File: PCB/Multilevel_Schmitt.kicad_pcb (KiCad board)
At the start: 2 copper layers, 32 x 102 mm, 24 parts, among them J1 Conn_02x03_Counter_Clockwise, J2 Conn_01x03, J3 Conn_01x08_Female, J4 Conn_01x08_Female, J5 Conn_01x02, Q1 BS170, U1 ATtiny84-20PU, U2 74HC14, U3 MCP1700-2502E_TO92, U4 74HC4051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

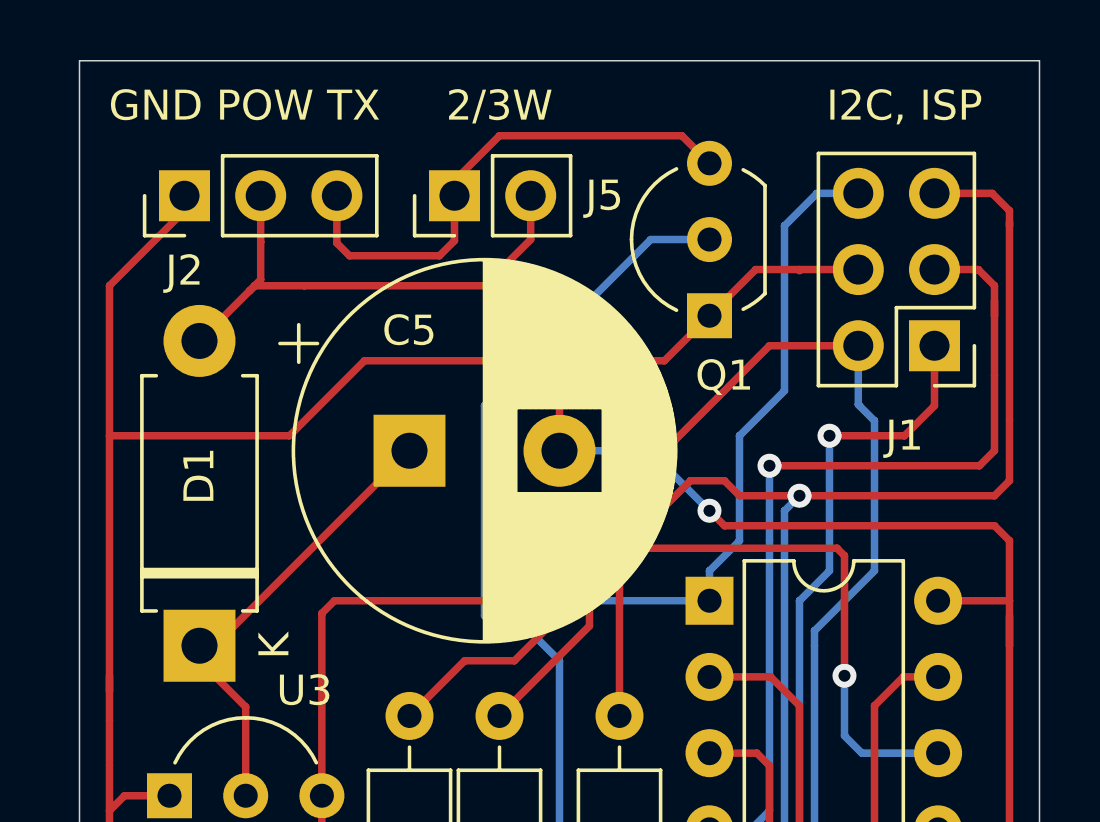
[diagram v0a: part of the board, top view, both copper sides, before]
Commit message: large cap holes
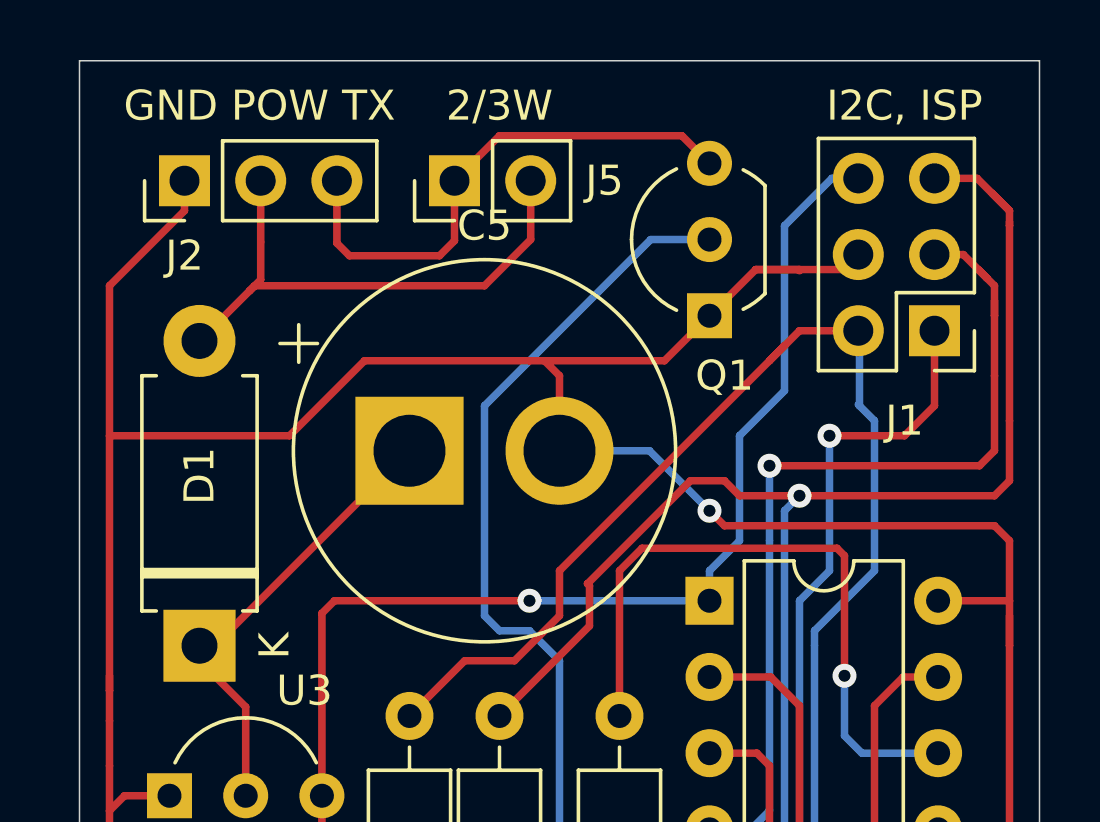
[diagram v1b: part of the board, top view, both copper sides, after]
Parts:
- C5: footprint Capacitor_THT:CP_Radial_D12.5mm_P5.00mm -> PCB:CP_Radial_D12.5mm_P5.00mm_LargePins
- moved J1 0.50 mm to (128.5, 54.0)
- moved J2 0.50 mm to (103.5, 49.0)
- moved J5 0.50 mm to (112.5, 49.0)
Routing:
- net M0: track 251.9 -> 254.6 mm
- net SCL_SCK: track 50.7 -> 49.0 mm
- net SDA_MOSI: track 54.2 -> 55.2 mm
- net Net-(D1-Pad2): track 17.2 -> 18.2 mm
- net RESET: track 29.7 -> 30.3 mm
- net MISO: track 31.5 -> 32.0 mm
